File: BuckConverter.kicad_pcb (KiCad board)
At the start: 2 copper layers, 23.3 x 26.4 mm, 16 parts, among them U1 LT1936IMS8E

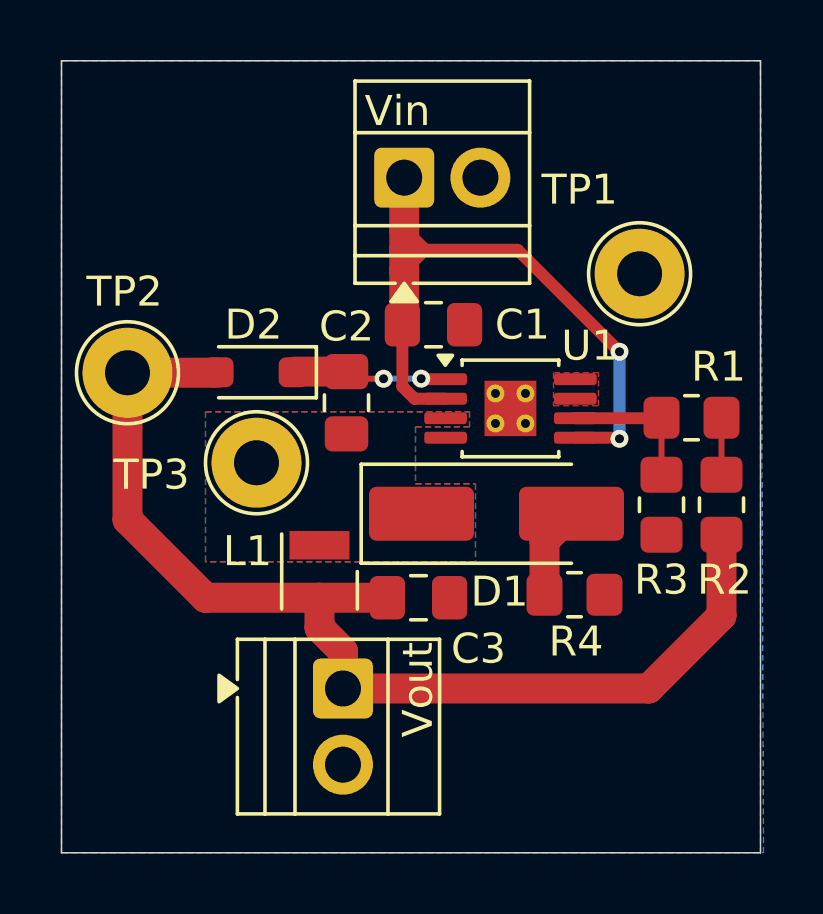
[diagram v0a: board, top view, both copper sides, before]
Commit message: place some via's, DRC fully OK TODO: check silkscreens/via overlap, fix thermal via placements
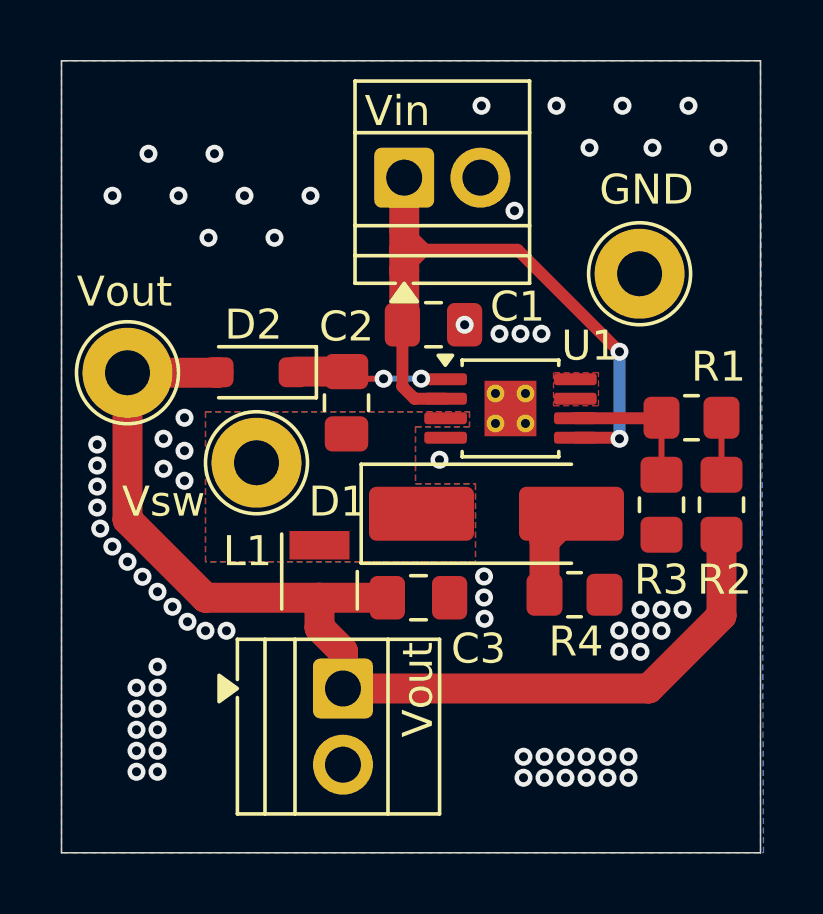
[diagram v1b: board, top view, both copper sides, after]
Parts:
- renumbered TP1 to GND, TP2 to Vout, TP3 to Vsw
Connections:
- U1 pad 9: (no net) -> GND
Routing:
- net GND: vias 0 -> 73
